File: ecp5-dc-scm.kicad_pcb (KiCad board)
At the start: 8 copper layers, 90 x 120.4 mm, 458 parts, among them IC1 TPS54561, J1 L834-1G1T-S7, J2 1-2199230-6, J3 529910408, J4 M20-7830642, J5 SFF-TA-1002-4C+, J6 0878311420, J7 61300611121, J8 S2B-PH-K-S_LF__SN_, Q1 2N7002, Q10 2N7002, Q11 2N7002, Q12 2N7002, Q13 2N7002, Q14 2N7002, Q15 2N7002, Q16 2N7002, Q17 2N7002, Q2 2N7002, Q3 2N7002, U1 KSZ9031RNXCA, U10 AS4C256M16D3, U11 TPS51200DRC, U12 LM3881MME_NOPB, U13 LM21212-2, U14 AMJMEFB-100.0000T, U16 TPS62823DLCT, U17 TPS62823DLCT, U18 TPS62823DLCT, U19 TPS62823DLCT, U2 W25Q32JVSSIQ_TR, U20 TPS62823DLCT, U21 ECP5UM5G_85_CABGA756, U3 W25Q32JVSSIQ_TR, U4 W25Q32JVSSIQ_TR, U5 W25Q32JVSSIQ_TR, U6 MTFC32GAPALBH-AIT, U7 NVT2008DQ,115, U8 USB3300-EZK-TR, U9 USB3300-EZK-TR, Y1 ABM8G-25.000MHZ-18-D2Y-T, Y2 TSX-3225, Y3 TSX-3225

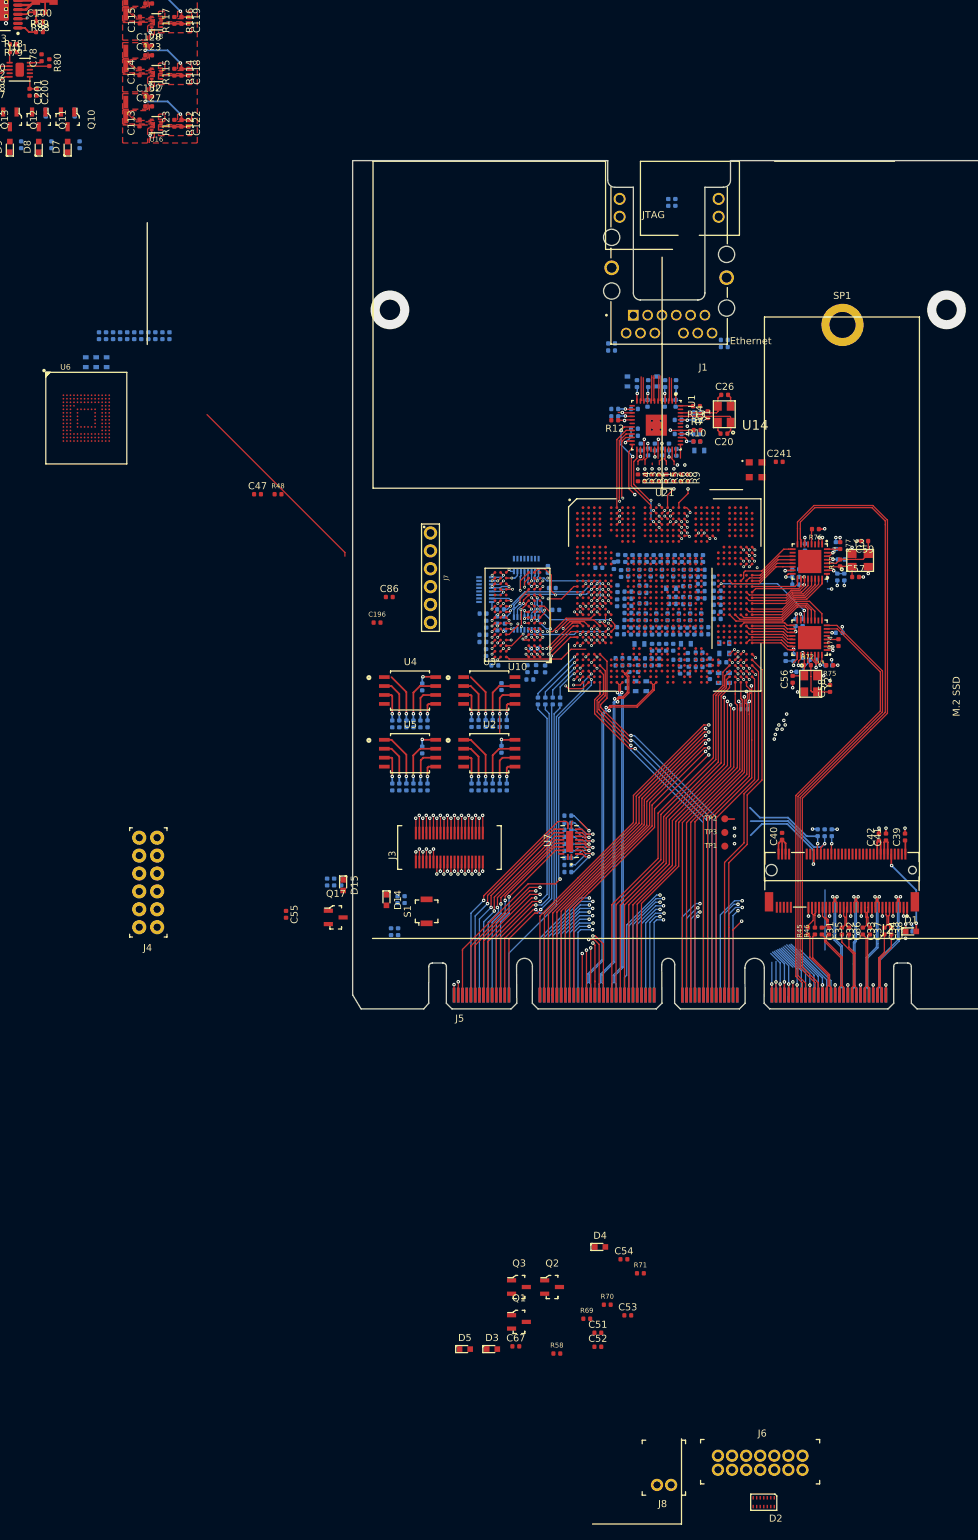
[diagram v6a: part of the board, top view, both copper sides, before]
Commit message: I2C routed
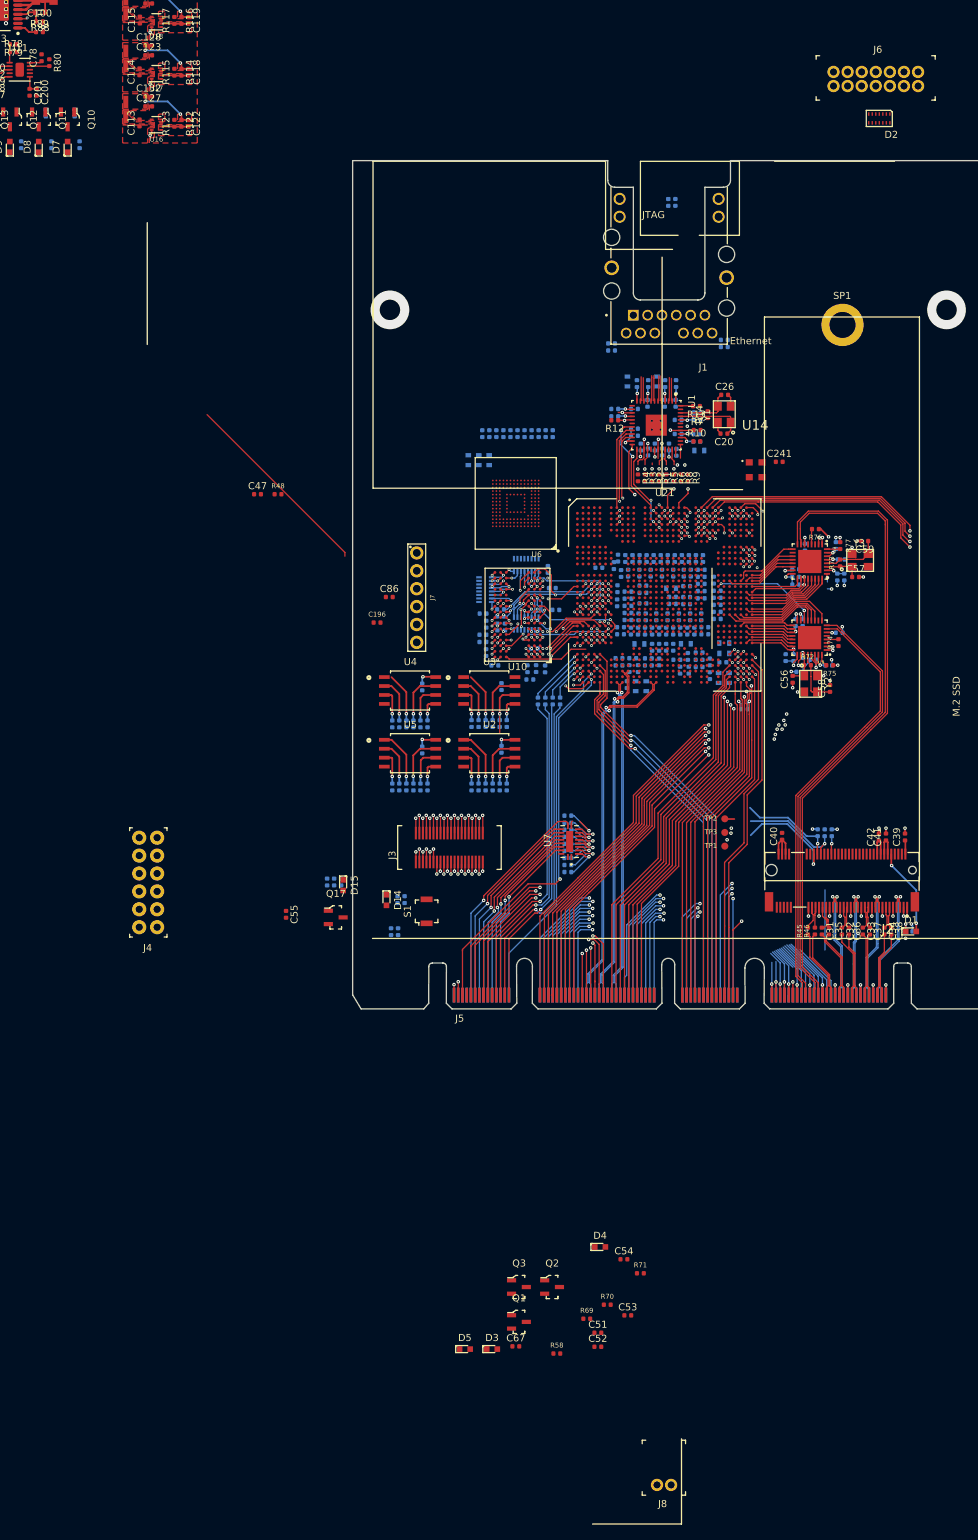
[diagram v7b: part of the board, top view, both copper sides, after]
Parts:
- moved D2 197.1 mm to (134.9, 52.9)
- moved J6 197.1 mm to (140.4, 46.3)
- moved R11 65.9 mm to (88.5, 97.7), turned to 270 degrees
- moved R59 63.9 mm to (87.5, 97.7), turned to 90 degrees
- moved U6 62.1 mm to (83.2, 107.5), turned to 180 degrees
- moved R60 62.0 mm to (86.5, 97.7), turned to 90 degrees
- moved R61 60.0 mm to (85.5, 97.7), turned to 90 degrees
- moved R62 58.1 mm to (84.5, 97.7), turned to 90 degrees
- moved R63 56.1 mm to (83.5, 97.7), turned to 90 degrees
- moved C48 56.1 mm to (79.5, 101.4)
- moved C49 56.1 mm to (76.5, 101.4)
- moved C50 56.1 mm to (78.0, 101.4)
- moved R64 54.2 mm to (82.5, 97.7), turned to 90 degrees
- moved R65 52.3 mm to (81.5, 97.7), turned to 90 degrees
- moved R66 50.4 mm to (80.5, 97.7), turned to 90 degrees
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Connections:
- U21 pad A23: I2C[10]_SDA -> I2C[12]_SDA
- U21 pad A24: I2C[9]_SCL -> I2C[12]_SCL
- U21 pad A25: I2C[7]_SCL -> I2C[11]_SDA
- U21 pad A26: I2C[5]_SDA -> I2C[11]_SCL
- U21 pad A28: I2C[3]_SDA -> I2C[7]_SCL
- U21 pad A29: I2C[2]_SDA -> I2C[6]_SDA
- U21 pad A30: I2C[1]_SCL -> I2C[6]_SCL
- U21 pad A31: I2C[0]_SCL -> I2C[5]_SCL
- U21 pad B22: I2C[8]_SDA -> I2C[10]_SDA
- U21 pad B23: I2C[12]_SDA -> I2C[10]_SCL
- U21 pad B25: I2C[6]_SCL -> I2C[8]_SCL
- U21 pad B26: I2C[4]_SDA -> I2C[8]_SDA
- U21 pad B29: I2C[1]_SDA -> I2C[4]_SDA
- U21 pad B30: I2C[0]_SDA -> I2C[5]_SDA
- U21 pad C23: I2C[11]_SCL -> I2C[9]_SCL
- U21 pad C24: I2C[8]_SCL -> I2C[9]_SDA
- U21 pad C26: I2C[3]_SCL -> I2C[4]_SCL
- U21 pad D22: I2C[4]_SCL -> I2C[2]_SCL
- U21 pad D23: I2C[10]_SCL -> I2C[2]_SDA
- U21 pad D24: I2C[9]_SDA -> I2C[3]_SDA
- U21 pad D25: I2C[6]_SDA -> I2C[3]_SCL
- U21 pad D26: I2C[2]_SCL -> I2C[0]_SDA
- U21 pad E22: I2C[12]_SCL -> I2C[1]_SCL
- U21 pad E23: I2C[11]_SDA -> I2C[1]_SDA
- U21 pad E25: I2C[5]_SCL -> I2C[0]_SCL
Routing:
- net (no net): track 145.2 -> 49.1 mm
- net I2C[6]_SCL: track 54.6 -> 106.2 mm, vias 1 -> 2
- net SGPIO_INTR_N: track 100.6 -> 50.4 mm
- net I2C[5]_SCL: track 55.7 -> 104.5 mm, vias 1 -> 2
- net SGPIO_RESET_N: track 97.3 -> 49.2 mm
- net I2C[12]_SDA: track 92.0 -> 109.8 mm, vias 1 -> 2
- net I2C[10]_SDA: track 95.2 -> 112.8 mm, vias 1 -> 2
- net I2C[9]_SCL: track 96.3 -> 112.5 mm, vias 1 -> 2
- net I2C[12]_SCL: track 92.5 -> 108.6 mm, vias 1 -> 2
- net I2C[10]_SCL: track 95.5 -> 111.5 mm, vias 1 -> 2
- net I2C[9]_SDA: track 96.1 -> 111.6 mm, vias 1 -> 2
- net I2C[11]_SDA: track 93.0 -> 107.5 mm, vias 1 -> 2
- net I2C[11]_SCL: track 93.7 -> 106.0 mm, vias 1 -> 2
- net I2C[8]_SCL: track 99.9 -> 111.6 mm, vias 1 -> 2
- net I2C[8]_SDA: track 99.6 -> 110.8 mm, vias 1 -> 2
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
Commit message: Started sketching MMC
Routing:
- net MMC_CMD: track 0.00 -> 15.4 mm, vias 0 -> 1
- net MMC_CLK: track 0.00 -> 14.6 mm, vias 0 -> 2
- net MMC_DAT6: track 0.00 -> 14.1 mm, vias 0 -> 1
- net MMC_DAT7: track 0.00 -> 13.5 mm, vias 0 -> 1
- net MMC_DAT4: track 0.00 -> 12.3 mm, vias 0 -> 1
- net MMC_DAT5: track 0.00 -> 12.2 mm, vias 0 -> 1
- net MMC_DAT3: track 0.00 -> 10.4 mm, vias 0 -> 1
- net GND: track 108.0 -> 108.6 mm, vias 95 -> 96
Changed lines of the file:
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@@
     (thickness 1.57)
     (drawings 80)
-    (tracks 3757)
+    (tracks 3801)
     (zones 0)
     (modules 458)
@@
   (segment (start 59 114.514256) (end 39.435744 94.95) (width 0.1) (layer F.Cu) (net 0))
   (segment (start 59 115.05) (end 59 114.514256) (width 0.1) (layer F.Cu) (net 0))
+  (via (at 95.6 114.95) (size 0.4) (drill 0.2) (layers F.Cu B.Cu) (net 1))
+  (segment (start 95.2 114.55) (end 95.6 114.95) (width 0.15) (layer F.Cu) (net 1))
+  (via (at 95.6 113.35) (size 0.4) (drill 0.2) (layers F.Cu B.Cu) (net 356))
+  (segment (start 96 113.75) (end 95.6 113.35) (width 0.15) (layer F.Cu) (net 356))
+  (via (at 95.6 114.15) (size 0.4) (drill 0.2) (layers F.Cu B.Cu) (net 354))
+  (segment (start 96 114.55) (end 95.6 114.15) (width 0.15) (layer F.Cu) (net 354))
+  (via (at 96.4 114.15) (size 0.4) (drill 0.2) (layers F.Cu B.Cu) (net 355))
+  (segment (start 96.8 114.55) (end 96.4 114.15) (width 0.15) (layer F.Cu) (net 355))
+  (via (at 96.4 114.95) (size 0.4) (drill 0.2) (layers F.Cu B.Cu) (net 351))
+  (segment (start 96.8 115.35) (end 96.4 114.95) (width 0.15) (layer F.Cu) (net 351))
+  (via (at 95.6 115.75) (size 0.4) (drill 0.2) (layers F.Cu B.Cu) (net 353))
+  (segment (start 96 115.35) (end 95.6 115.75) (width 0.15) (layer F.Cu) (net 353))
+  (via (at 94.8 115.75) (size 0.4) (drill 0.2) (layers F.Cu B.Cu) (net 352))
+  (segment (start 95.2 115.35) (end 94.8 115.75) (width 0.15) (layer F.Cu) (net 352))
+  (via (at 94 115.75) (size 0.4) (drill 0.2) (layers F.Cu B.Cu) (net 350))
+  (segment (start 94.4 116.15) (end 94 115.75) (width 0.15) (layer F.Cu) (net 350))
+  (via (at 93.2 115.75) (size 0.4) (drill 0.2) (layers F.Cu B.Cu) (net 356))
+  (segment (start 93.6 116.15) (end 93.2 115.75) (width 0.15) (layer F.Cu) (net 356))
   (via (at 109.2 109.35) (size 0.4) (drill 0.2) (layers F.Cu B.Cu) (net 45))
   (segment (start 109.6 109.75) (end 109.2 109.35) (width 0.15) (layer F.Cu) (net 45))
@@
   (via (at 113.25 155.3) (size 0.5) (drill 0.2) (layers F.Cu B.Cu) (net 328))
   (via (at 113.85 153.65) (size 0.5) (drill 0.2) (layers F.Cu B.Cu) (net 330))
+  (segment (start 94 115.75) (end 93.55 115.3) (width 0.1) (layer In2.Cu) (net 350))
+  (segment (start 93.55 115.3) (end 90.55 115.3) (width 0.1) (layer In2.Cu) (net 350))
+  (segment (start 90.55 115.3) (end 86.25 111) (width 0.1) (layer In2.Cu) (net 350))
+  (segment (start 86.25 111) (end 86.2 110.95) (width 0.1) (layer In2.Cu) (net 350))
+  (segment (start 90.2 114.55) (end 86.65 111) (width 0.1) (layer In2.Cu) (net 351))
+  (segment (start 96.4 114.95) (end 96 115.35) (width 0.1) (layer In2.Cu) (net 351))
+  (segment (start 94.35 115.35) (end 93.55 114.55) (width 0.1) (layer In2.Cu) (net 351))
+  (segment (start 96 115.35) (end 94.35 115.35) (width 0.1) (layer In2.Cu) (net 351))
+  (segment (start 93.55 114.55) (end 90.2 114.55) (width 0.1) (layer In2.Cu) (net 351))
+  (segment (start 94.8 115.75) (end 94.8 115.8) (width 0.1) (layer In2.Cu) (net 352))
+  (segment (start 94.8 115.8) (end 94.45 116.15) (width 0.1) (layer In2.Cu) (net 352))
+  (segment (start 94.45 116.15) (end 90.9 116.15) (width 0.1) (layer In2.Cu) (net 352))
+  (segment (start 90.9 116.15) (end 85.6 110.85) (width 0.1) (layer In2.Cu) (net 352))
+  (segment (start 90.65 116.4) (end 84.8 110.55) (width 0.1) (layer In2.Cu) (net 353))
+  (segment (start 95.6 115.75) (end 94.95 116.4) (width 0.1) (layer In2.Cu) (net 353))
+  (segment (start 94.95 116.4) (end 90.65 116.4) (width 0.1) (layer In2.Cu) (net 353))
+  (segment (start 95.6 114.15) (end 90.65 114.15) (width 0.1) (layer In2.Cu) (net 354))
+  (segment (start 90.65 114.15) (end 86.55 110.05) (width 0.1) (layer In2.Cu) (net 354))
+  (segment (start 86.55 110.05) (end 84.35 110.05) (width 0.1) (layer In2.Cu) (net 354))
+  (segment (start 96.4 114.15) (end 96.35 114.1) (width 0.1) (layer In2.Cu) (net 355))
+  (segment (start 96.35 114.1) (end 96.35 113.45) (width 0.1) (layer In2.Cu) (net 355))
+  (segment (start 96.35 113.45) (end 95.8 112.9) (width 0.1) (layer In2.Cu) (net 355))
+  (segment (start 95.8 112.9) (end 91.3 112.9) (width 0.1) (layer In2.Cu) (net 355))
+  (segment (start 91.3 112.9) (end 85.05 106.65) (width 0.1) (layer In2.Cu) (net 355))
+  (segment (start 95.6 113.35) (end 91.35 113.35) (width 0.1) (layer In2.Cu) (net 356))
+  (segment (start 91.35 113.35) (end 84.85 106.85) (width 0.1) (layer In2.Cu) (net 356))
   (zone (net 0) (net_name "") (layers F.Cu GND1 In2.Cu VCC1 GND2 B.Cu) (hatch edge 0.508)
     (connect_pads (clearance 0.508))
